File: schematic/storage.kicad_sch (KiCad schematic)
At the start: 5 parts, among them J8 Conn_01x03, U4 6116XA, U5 AT27C256R-70JU-T

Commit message: update pdf schematic and schematic wording
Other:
- title: Righteous Tentacle, Colecovision Reverse Engineering Project -> Mini Colecovision
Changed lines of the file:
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@@
   (paper "USLetter")
   (title_block
-    (title "Righteous Tentacle, Colecovision Reverse Engineering Project")
-    (date "2023-06-18")
-    (rev "1.0.0.F")
+    (title "Mini Colecovision")
+    (date "2024-03-25")
+    (rev "1.0.0")
     (company "sparkletron")
     (comment 1 "Jay Convertino")
     (comment 2 "MIT LICENSE")
-    (comment 3 "PCB: 75743 REV F")
+    (comment 3 "TARGET: Portable")
   )
   (junction (at 139.7 59.055) (diameter 0) (color 0 0 0 0)

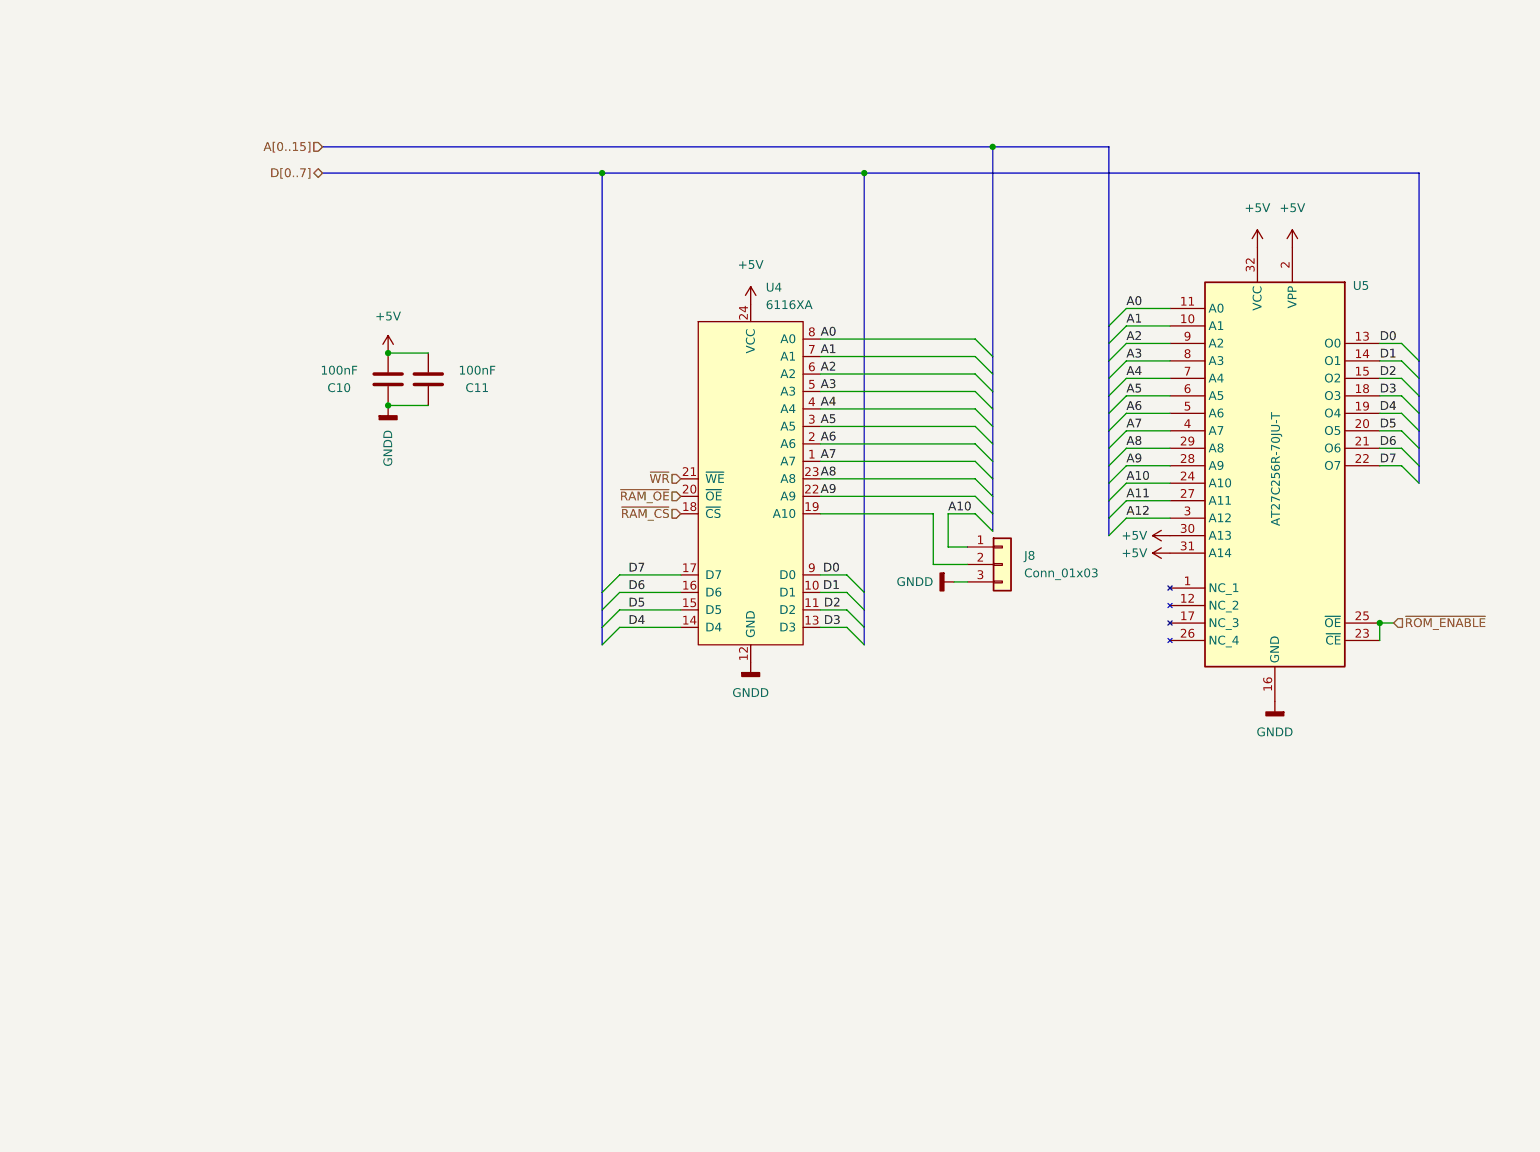
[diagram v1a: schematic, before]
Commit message: first commit with PCB revised for super game module. Needs model updates and tweaks
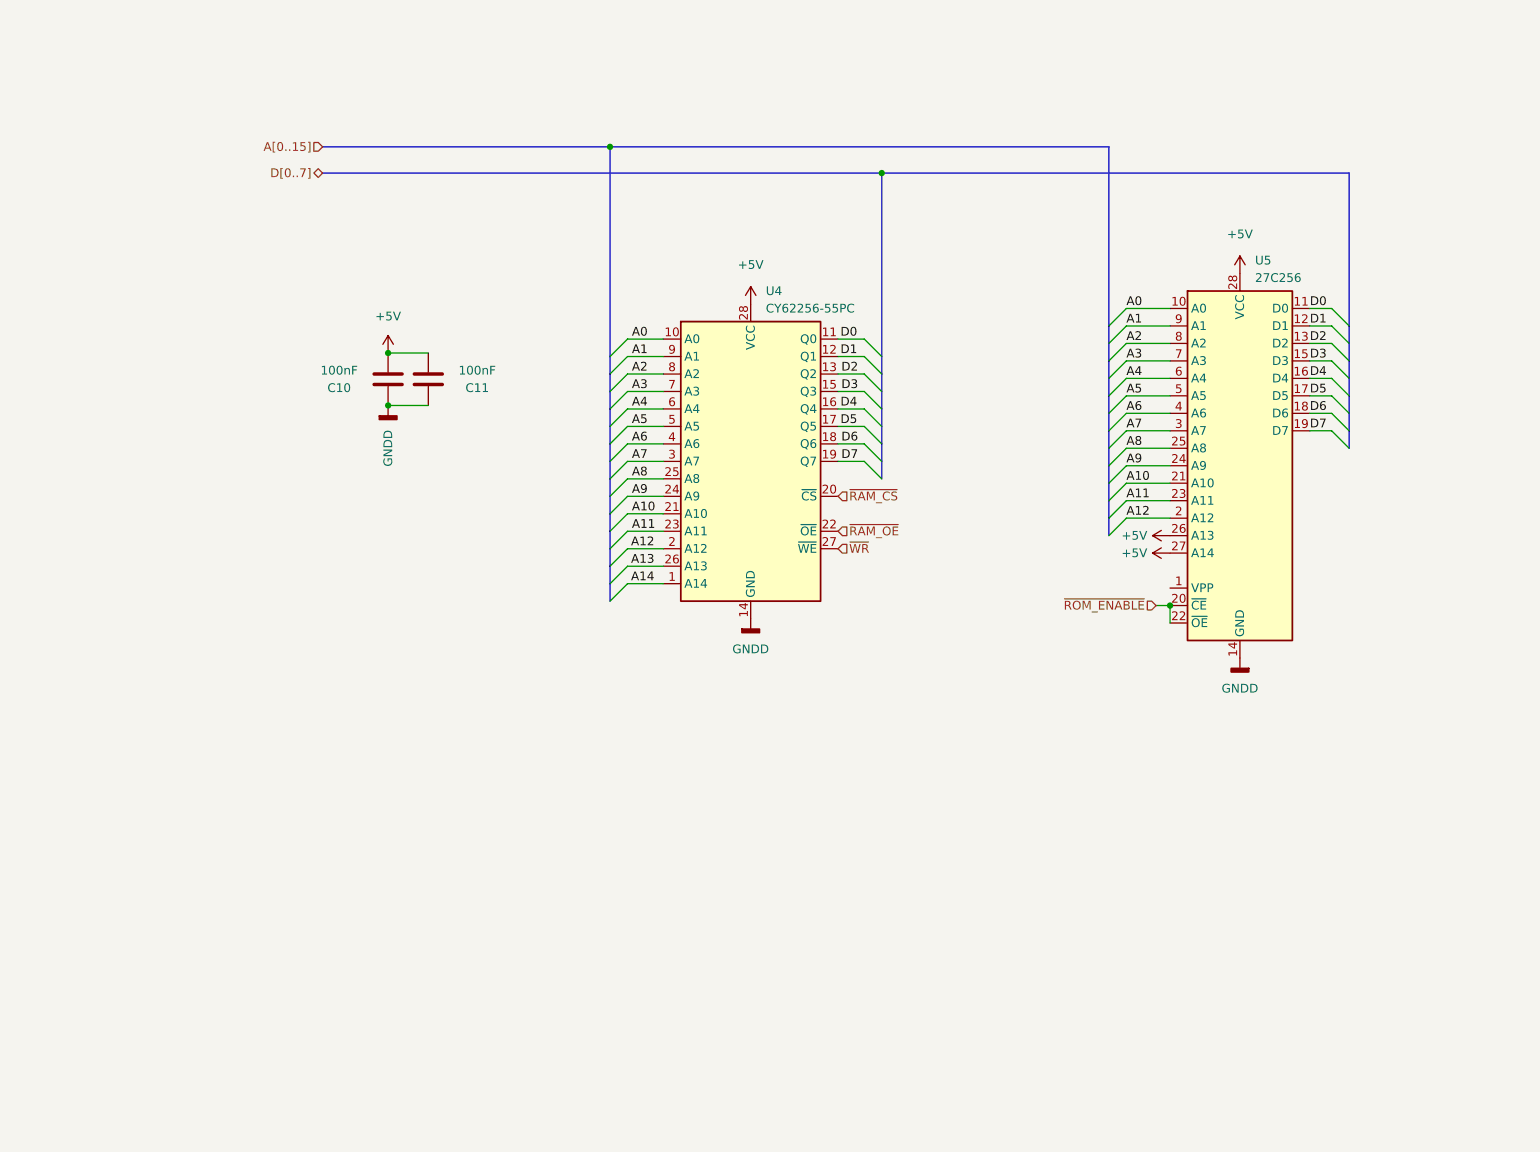
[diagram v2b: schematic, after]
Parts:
- removed J8: Conn_01x03, Connector_PinHeader_2.54mm:PinHeader_1x03_P2.54mm_Vertical, symbol Connector_Generic:Conn_01x03
- removed U4: 6116XA, Package_DIP:DIP-24_W7.62mm_LongPads, symbol Vintage_RAM:6116XA
- removed U5: AT27C256R-70JU-T, Package_LCC:PLCC-32_THT-Socket, symbol ROM_EXT:AT27C256R-70JU-T
- added U4: CY62256-55PC, Package_DIP:DIP-28_W15.24mm, symbol Memory_RAM:CY62256-70PC
- added U5: 27C256, Package_DIP:DIP-28_W15.24mm, symbol Memory_EPROM:27C256
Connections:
- net +5V: now also U4.28 (VCC), U5.26 (A13), U5.27 (A14), U5.28 (VCC)
- net A0: now also U4.10 (A0), U5.10 (A0)
- net A1: now also U4.9 (A1), U5.9 (A1)
- net A10: now also U4.21 (A10), U5.21 (A10)
- net A11: now also U4.23 (A11), U5.23 (A11)
- net A12: now also U4.2 (A12), U5.2 (A12)
- net A2: now also U4.8 (A2), U5.8 (A2)
- net A3: now also U4.7 (A3), U5.7 (A3)
- net A4: now also U4.6 (A4), U5.6 (A4)
- net A5: now also U4.5 (A5), U5.5 (A5)
- net A6: now also U4.4 (A6), U5.4 (A6)
- net A7: now also U4.3 (A7), U5.3 (A7)
- net A8: now also U4.25 (A8), U5.25 (A8)
- net A9: now also U4.24 (A9), U5.24 (A9)
- net D0: now also U4.11 (Q0), U5.11 (D0)
- net D1: now also U4.12 (Q1), U5.12 (D1)
- net D2: now also U4.13 (Q2), U5.13 (D2)
- net D3: now also U4.15 (Q3), U5.15 (D3)
- net D4: now also U4.16 (Q4), U5.16 (D4)
- net D5: now also U4.17 (Q5), U5.17 (D5)
- net D6: now also U4.18 (Q6), U5.18 (D6)
- net D7: now also U4.19 (Q7), U5.19 (D7)
- net GNDD: now also U4.14 (GND), U5.14 (GND)
- net ~{RAM_CS}: now also U4.20 (~{CS})
- net ~{RAM_OE}: now also U4.22 (~{OE})
- net ~{ROM_ENABLE}: now also U5.20 (~{CE}), U5.22 (~{OE})
- net ~{WR}: now also U4.27 (~{WE})
- new net A13: U4.26 (A13)
- new net A14: U4.1 (A14)

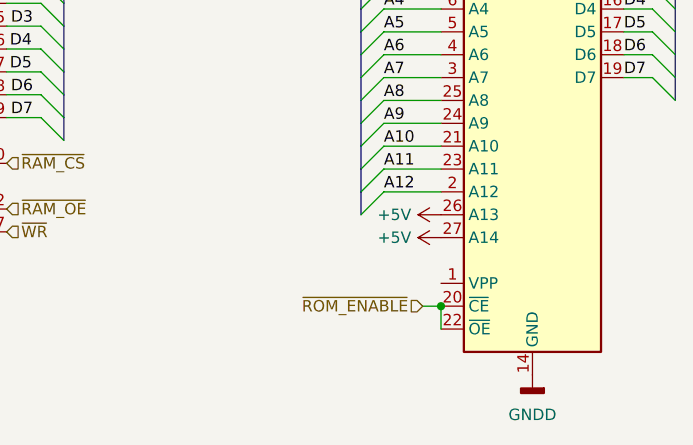
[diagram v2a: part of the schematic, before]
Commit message: updated output jacks to correct footprint
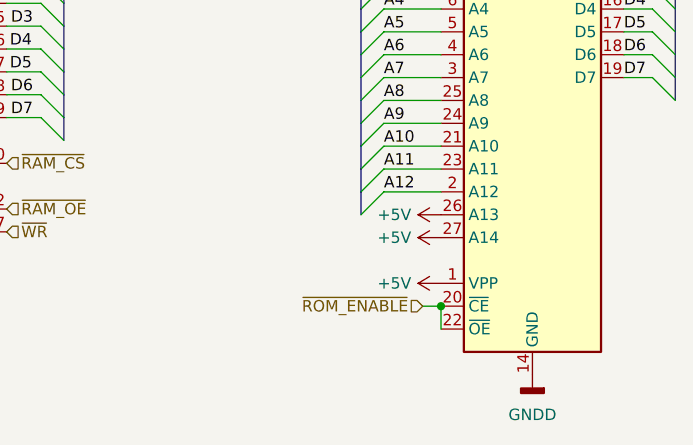
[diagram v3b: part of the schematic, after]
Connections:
- net +5V: now also U5.1 (VPP)
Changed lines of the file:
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@@
+    )
+  )
+  (symbol (lib_id "power:+5V") (at 184.15 119.38 90) (mirror x) (unit 1)
+    (in_bom yes) (on_board yes) (dnp no) (fields_autoplaced)
+    (property "Reference" "#PWR088" (at 187.96 119.38 0)
+      (effects (font (size 1.27 1.27)) hide)
+    )
+    (property "Value" "+5V" (at 180.848 119.38 90)
+      (effects (font (size 1.27 1.27)) (justify left))
+    )
+    (property "Footprint" "" (at 184.15 119.38 0)
+      (effects (font (size 1.27 1.27)) hide)
+    )
+    (property "Datasheet" "" (at 184.15 119.38 0)
+      (effects (font (size 1.27 1.27)) hide)
+    )
+    (pin "1")
+    (instances
+      (project "coleco_original"
+        (path "/970e0f64-111f-41e3-9f5a-fb0d0f6fa101/00000000-0000-0000-0000-00006262cd34"
+          (reference "#PWR088") (unit 1)
+        )
+      )
     )
   )

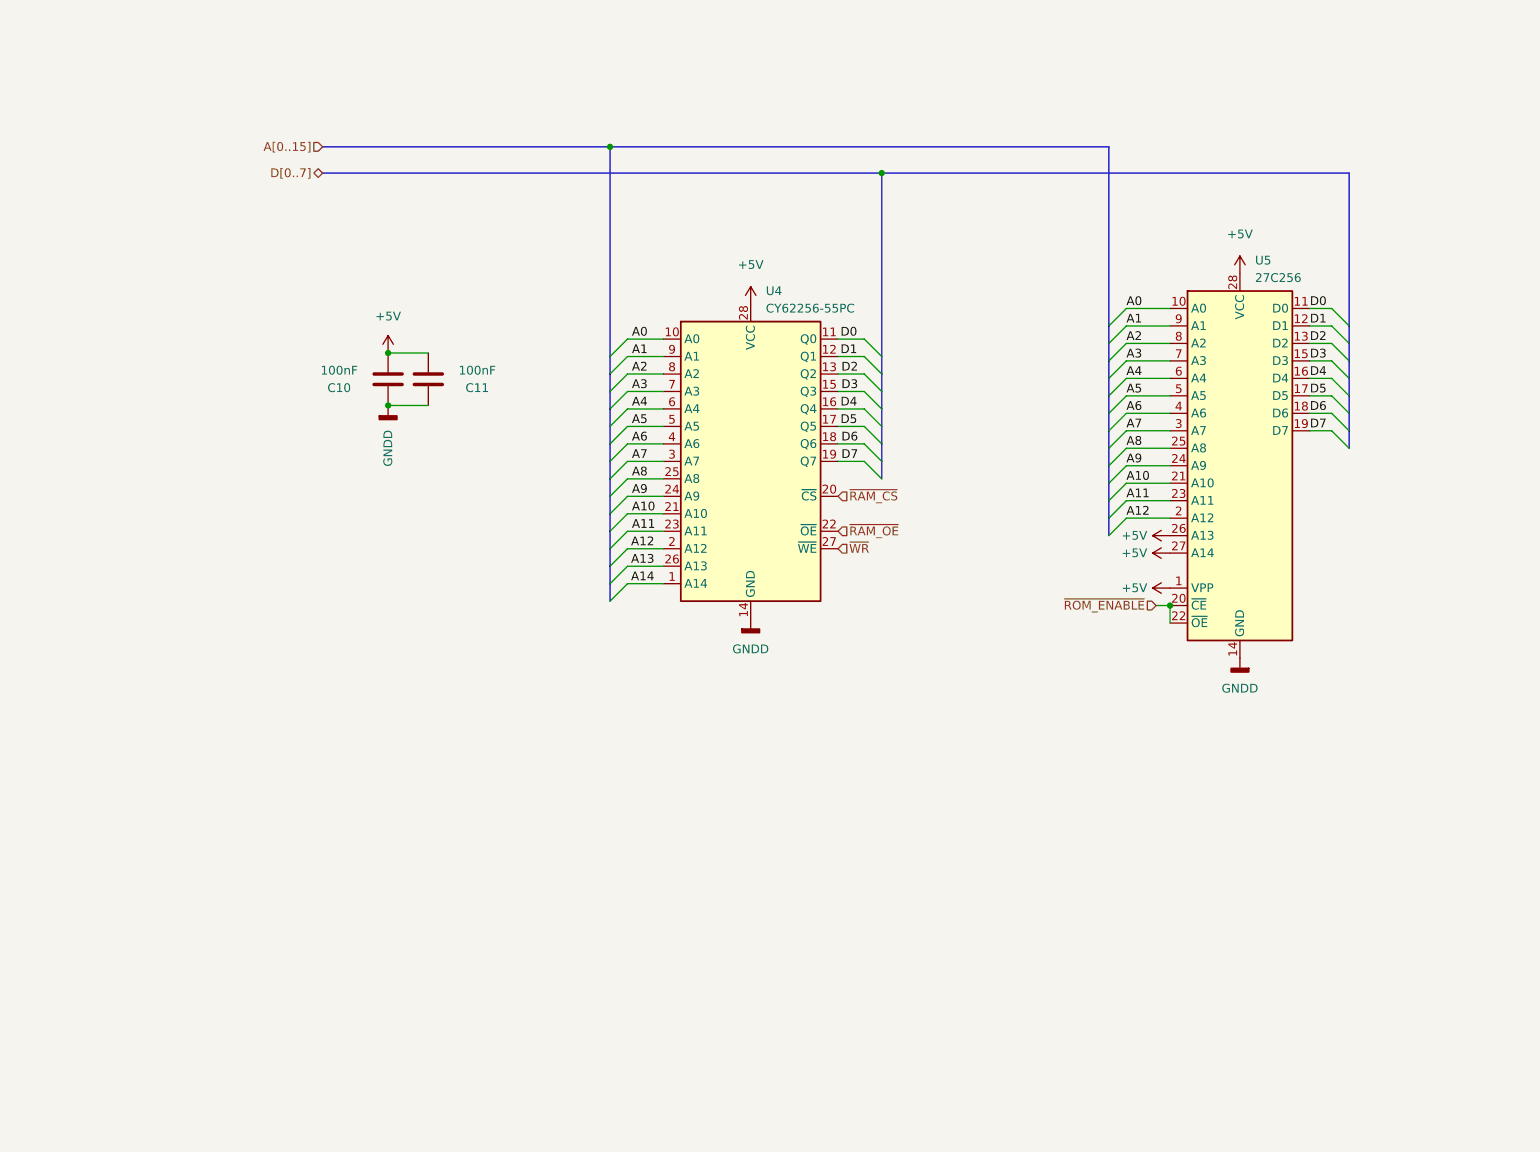
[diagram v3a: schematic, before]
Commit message: complete ram mirror when banks not enabled.
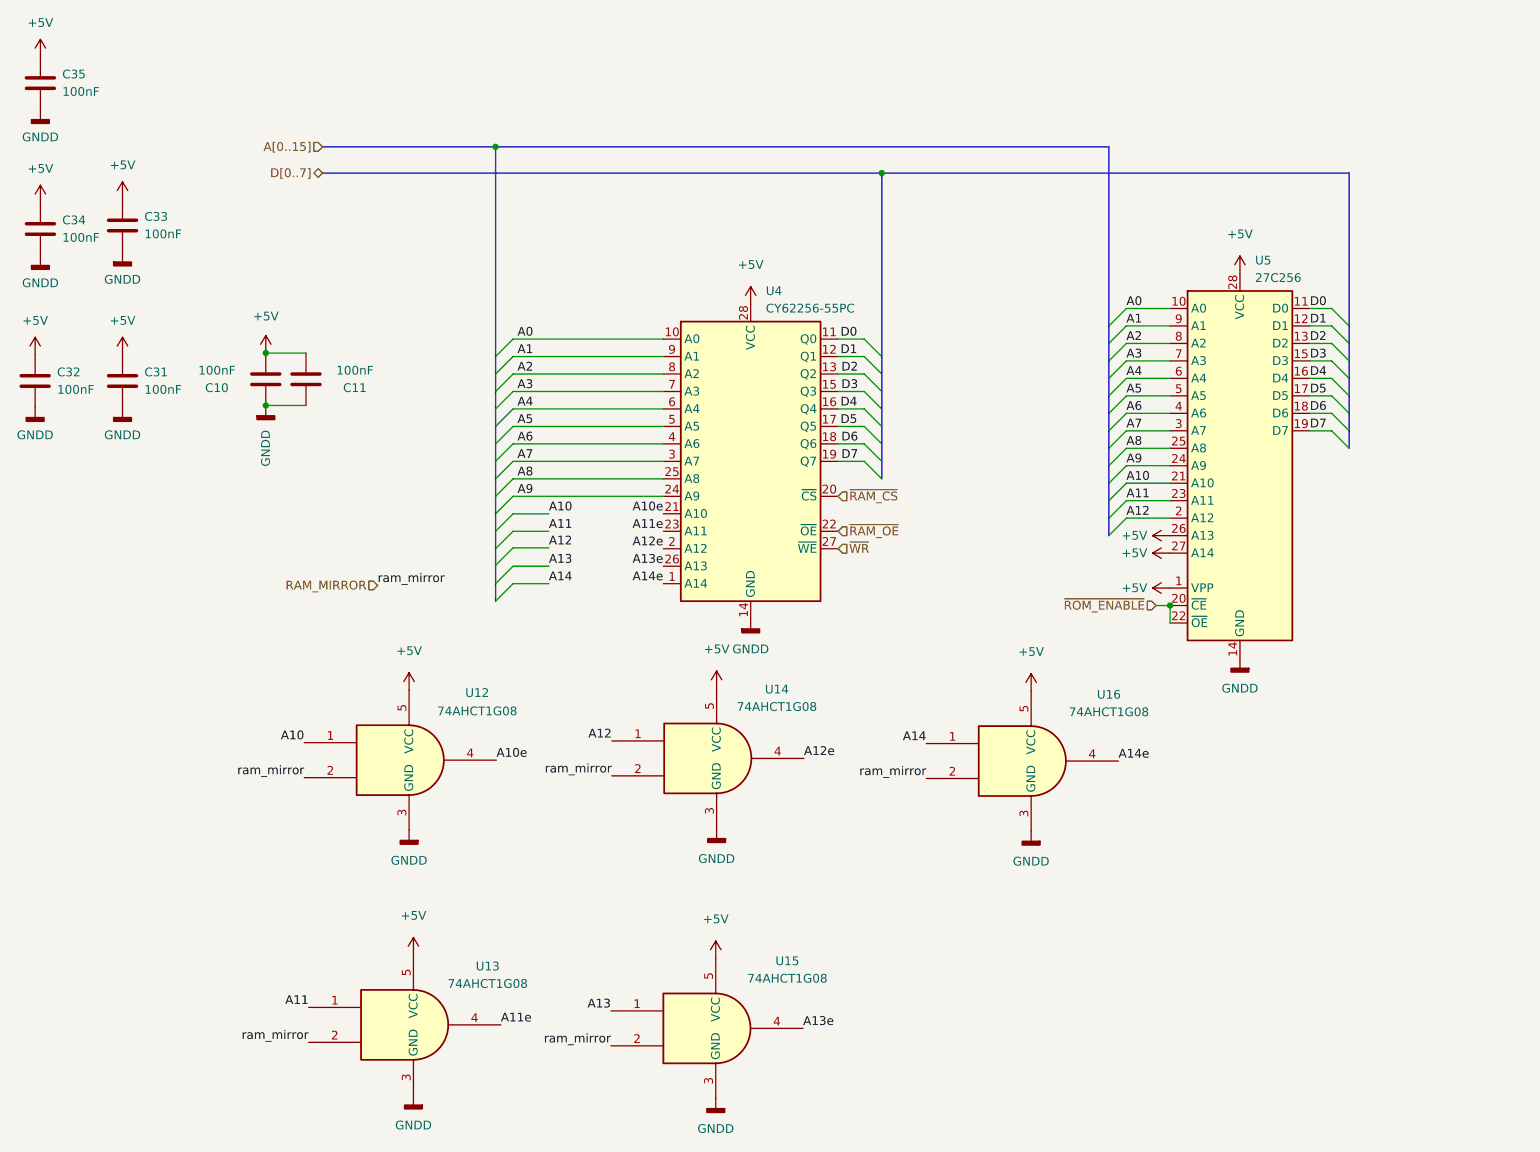
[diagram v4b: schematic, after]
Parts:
- added C31, C32, C33, C34, C35: 100nF, Capacitor_SMD:C_1206_3216Metric, symbol Device:C
- added U12, U13, U14, U15, U16: 74AHCT1G08, Package_TO_SOT_SMD:SOT-23-5_HandSoldering, symbol 74xGxx:74AHCT1G08
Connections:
- net +5V: now also C31.1, C32.1, C33.1, C34.1, C35.1, U12.5 (VCC), U13.5 (VCC), U14.5 (VCC), U15.5 (VCC), U16.5 (VCC)
- net A10: now also U12.1; no longer U4.21 (A10)
- net A11: now also U13.1; no longer U4.23 (A11)
- net A12: now also U14.1; no longer U4.2 (A12)
- net A13: now also U15.1; no longer U4.26 (A13)
- net A14: now also U16.1; no longer U4.1 (A14)
- net GNDD: now also C31.2, C32.2, C33.2, C34.2, C35.2, U12.3 (GND), U13.3 (GND), U14.3 (GND), U15.3 (GND), U16.3 (GND)
- new net A10e: U12.4, U4.21 (A10)
- new net A11e: U13.4, U4.23 (A11)
- new net A12e: U14.4, U4.2 (A12)
- new net A13e: U15.4, U4.26 (A13)
- new net A14e: U16.4, U4.1 (A14)
- new net RAM_MIRROR: U12.2, U13.2, U14.2, U15.2, U16.2
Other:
- moved on the sheet: C10, C11
